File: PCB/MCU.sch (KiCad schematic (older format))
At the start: 18 parts, among them U6 TMS320F28035PAGS, U7 MB85RS16

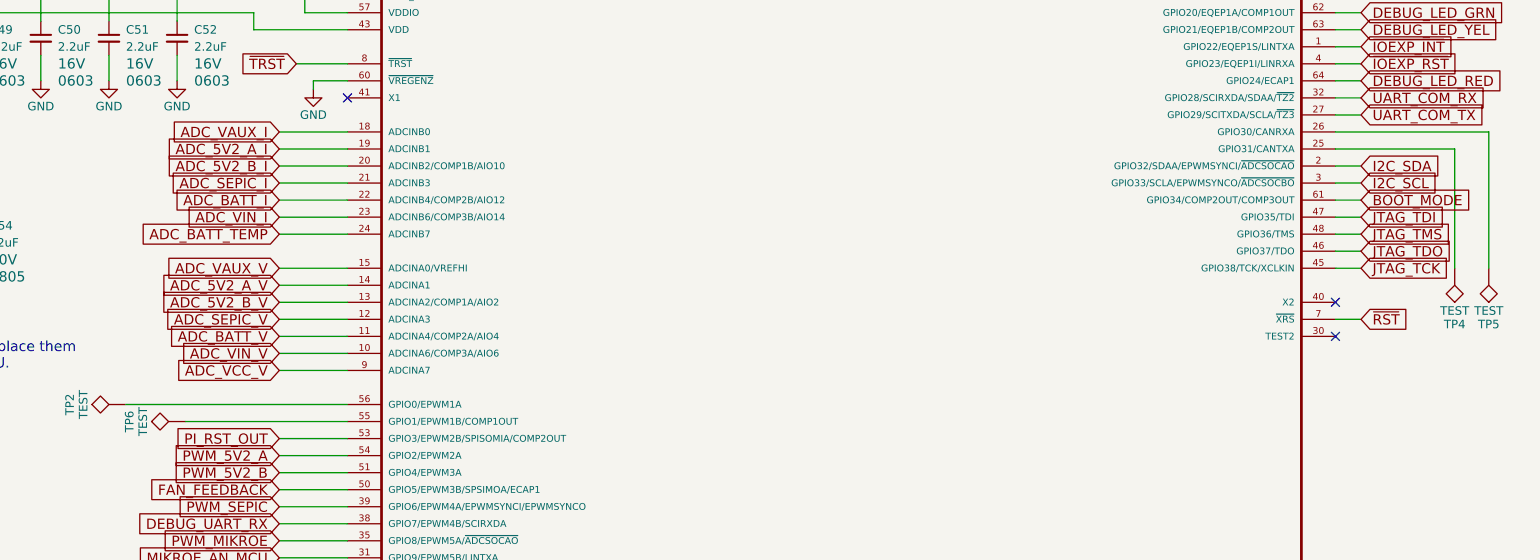
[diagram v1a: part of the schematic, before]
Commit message: Added ELOAD to sch and imported to layout
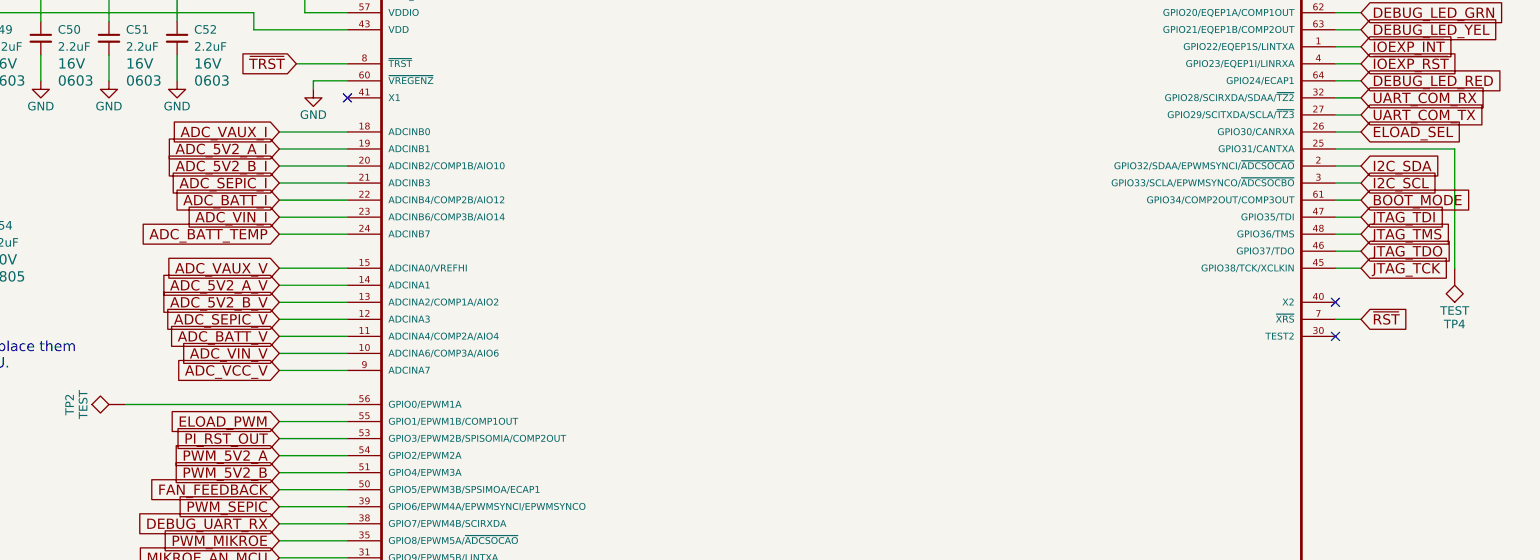
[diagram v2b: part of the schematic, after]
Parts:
- removed TP5, TP6: TEST, Measurement_Points:Measurement_Point_Round-SMD-Pad_Small, symbol TEST
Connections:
- net ELOAD_SEL: now reaches U6.26 (GPIO30/CANRXA)
- net ELOAD_PWM: now reaches U6.55 (GPIO1/EPWM1B/COMP1OUT)
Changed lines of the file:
@@
 $Descr A 11000 8500
 encoding utf-8
-Sheet 6 11
+Sheet 6 12
 Title "MCU"
 Date "2018-06-16"
-Rev "01"
+Rev "02"
 Comp ""
 Comment1 ""
@@
 $EndComp
 $Comp
-L GND #PWR098
+L GND #PWR0101
 U 1 1 5B2621C1
 P 700 1900
-F 0 "#PWR098" H 700 1650 50  0001 C CNN
+F 0 "#PWR0101" H 700 1650 50  0001 C CNN
 F 1 "GND" H 700 1750 50  0000 C CNN
 F 2 "" H 700 1900 50  0001 C CNN
@@
 $EndComp
 $Comp
-L GND #PWR099
+L GND #PWR0102
 U 1 1 5B2621FD
 P 1100 1900
-F 0 "#PWR099" H 1100 1650 50  0001 C CNN
+F 0 "#PWR0102" H 1100 1650 50  0001 C CNN
 F 1 "GND" H 1100 1750 50  0000 C CNN
 F 2 "" H 1100 1900 50  0001 C CNN
@@
 $EndComp
 $Comp
-L GND #PWR0100
+L GND #PWR0103
 U 1 1 5B26221D
 P 1500 1900
-F 0 "#PWR0100" H 1500 1650 50  0001 C CNN
+F 0 "#PWR0103" H 1500 1650 50  0001 C CNN
 F 1 "GND" H 1500 1750 50  0000 C CNN
 F 2 "" H 1500 1900 50  0001 C CNN
@@
 $EndComp
 $Comp
-L GND #PWR0101
+L GND #PWR0104
 U 1 1 5B26223D
 P 1900 1900
-F 0 "#PWR0101" H 1900 1650 50  0001 C CNN
+F 0 "#PWR0104" H 1900 1650 50  0001 C CNN
 F 1 "GND" H 1900 1750 50  0000 C CNN
 F 2 "" H 1900 1900 50  0001 C CNN
@@
 $EndComp
 $Comp
-L GND #PWR0102
+L GND #PWR0105
 U 1 1 5B26225D
 P 2300 1900
-F 0 "#PWR0102" H 2300 1650 50  0001 C CNN
+F 0 "#PWR0105" H 2300 1650 50  0001 C CNN
 F 1 "GND" H 2300 1750 50  0000 C CNN
 F 2 "" H 2300 1900 50  0001 C CNN
@@
 $EndComp
 $Comp
-L GND #PWR0103
+L GND #PWR0106
 U 1 1 5B26227D
 P 2700 1900
-F 0 "#PWR0103" H 2700 1650 50  0001 C CNN
+F 0 "#PWR0106" H 2700 1650 50  0001 C CNN
 F 1 "GND" H 2700 1750 50  0000 C CNN
 F 2 "" H 2700 1900 50  0001 C CNN
@@
 $EndComp
 $Comp
-L GND #PWR0104
+L GND #PWR0107
 U 1 1 5B2622CE
 P 3400 5750
-F 0 "#PWR0104" H 3400 5500 50  0001 C CNN
+F 0 "#PWR0107" H 3400 5500 50  0001 C CNN
 F 1 "GND" H 3400 5600 50  0000 C CNN
 F 2 "" H 3400 5750 50  0001 C CNN
@@
 Connection ~ 2700 1300
 $Comp
-L +3V3 #PWR0105
+L +3V3 #PWR0108
 U 1 1 5B26280D
 P 1900 1000
-F 0 "#PWR0105" H 1900 850 50  0001 C CNN
+F 0 "#PWR0108" H 1900 850 50  0001 C CNN
 F 1 "+3V3" H 1900 1140 50  0000 C CNN
 F 2 "" H 1900 1000 50  0001 C CNN
@@
 $EndComp
 $Comp
-L +3V3 #PWR0106
+L +3V3 #PWR0109
 U 1 1 5B26285E
 P 2300 1000
-F 0 "#PWR0106" H 2300 850 50  0001 C CNN
+F 0 "#PWR0109" H 2300 850 50  0001 C CNN
 F 1 "+3V3" H 2300 1140 50  0000 C CNN
 F 2 "" H 2300 1000 50  0001 C CNN
@@
 	9500 3300 9650 3300
 $Comp
-L GND #PWR0107
+L GND #PWR0110
 U 1 1 5B25830D
 P 3500 1950
-F 0 "#PWR0107" H 3500 1700 50  0001 C CNN
+F 0 "#PWR0110" H 3500 1700 50  0001 C CNN
 F 1 "GND" H 3500 1800 50  0000 C CNN
 F 2 "" H 3500 1950 50  0001 C CNN
@@
 Wire Wire Line
 	10200 1400 9500 1400
-$Comp
-L TEST TP5
-U 1 1 5B258786
-P 10400 3000
-F 0 "TP5" H 10400 3300 50  0000 C BNN
-F 1 "TEST" H 10400 3250 50  0000 C CNN
-F 2 "Measurement_Points:Measurement_Point_Round-SMD-Pad_Small" H 10400 3000 50  0001 C CNN
-F 3 "" H 10400 3000 50  0001 C CNN
-	1    10400 3000
-	-1   0    0    1
-$EndComp
 $Comp
 L TEST TP4
@@
 Wire Wire Line
 	10200 2300 10200 3000
-Wire Wire Line
-	9500 2200 10400 2200
-Wire Wire Line
-	10400 2200 10400 3000
-$Comp
-L TEST TP6
-U 1 1 5B258A6D
-P 2750 3900
-F 0 "TP6" H 2750 4200 50  0000 C BNN
-F 1 "TEST" H 2750 4150 50  0000 C CNN
-F 2 "Measurement_Points:Measurement_Point_Round-SMD-Pad_Small" H 2750 3900 50  0001 C CNN
-F 3 "" H 2750 3900 50  0001 C CNN
-	1    2750 3900
-	0    -1   -1   0
-$EndComp
-Wire Wire Line
-	2750 3900 3700 3900
 $Comp
 L C_Small C48
@@
 $EndComp
 $Comp
-L +3V3 #PWR0108
+L +3V3 #PWR0111
 U 1 1 5B25DAED
 P 800 2500
-F 0 "#PWR0108" H 800 2350 50  0001 C CNN
+F 0 "#PWR0111" H 800 2350 50  0001 C CNN
 F 1 "+3V3" H 800 2640 50  0000 C CNN
 F 2 "" H 800 2500 50  0001 C CNN
@@
 $EndComp
 $Comp
-L +3V3 #PWR0109
+L +3V3 #PWR0112
 U 1 1 5B25DB1F
 P 1500 2500
-F 0 "#PWR0109" H 1500 2350 50  0001 C CNN
+F 0 "#PWR0112" H 1500 2350 50  0001 C CNN
 F 1 "+3V3" H 1500 2640 50  0000 C CNN
 F 2 "" H 1500 2500 50  0001 C CNN
@@
 $EndComp
 $Comp
-L GND #PWR0110
+L GND #PWR0113
 U 1 1 5B25DB51
 P 800 3100
-F 0 "#PWR0110" H 800 2850 50  0001 C CNN
+F 0 "#PWR0113" H 800 2850 50  0001 C CNN
 F 1 "GND" H 800 2950 50  0000 C CNN
 F 2 "" H 800 3100 50  0001 C CNN
@@
 $EndComp
 $Comp
-L GND #PWR0111
+L GND #PWR0114
 U 1 1 5B25DB83
 P 1500 3100
-F 0 "#PWR0111" H 1500 2850 50  0001 C CNN
+F 0 "#PWR0114" H 1500 2850 50  0001 C CNN
 F 1 "GND" H 1500 2950 50  0000 C CNN
 F 2 "" H 1500 3100 50  0001 C CNN
@@
 $EndComp
 $Comp
-L GND #PWR0112
+L GND #PWR0115
 U 1 1 5B2606BF
 P 2900 7500
-F 0 "#PWR0112" H 2900 7250 50  0001 C CNN
+F 0 "#PWR0115" H 2900 7250 50  0001 C CNN
 F 1 "GND" H 2900 7350 50  0000 C CNN
 F 2 "" H 2900 7500 50  0001 C CNN
@@
 $EndComp
 $Comp
-L +3V3 #PWR0113
+L +3V3 #PWR0116
 U 1 1 5B26090E
 P 2900 6550
-F 0 "#PWR0113" H 2900 6400 50  0001 C CNN
+F 0 "#PWR0116" H 2900 6400 50  0001 C CNN
 F 1 "+3V3" H 2900 6690 50  0000 C CNN
 F 2 "" H 2900 6550 50  0001 C CNN
@@
 $EndComp
 $Comp
-L GND #PWR0114
+L GND #PWR0117
 U 1 1 5B260A81
 P 3800 6700
-F 0 "#PWR0114" H 3800 6450 50  0001 C CNN
+F 0 "#PWR0117" H 3800 6450 50  0001 C CNN
 F 1 "GND" H 3800 6550 50  0000 C CNN
 F 2 "" H 3800 6700 50  0001 C CNN
@@
 Connection ~ 1850 7000
 $Comp
-L +3V3 #PWR0115
+L +3V3 #PWR0118
 U 1 1 5B2E79A7
 P 1850 6350
-F 0 "#PWR0115" H 1850 6200 50  0001 C CNN
+F 0 "#PWR0118" H 1850 6200 50  0001 C CNN
 F 1 "+3V3" H 1850 6490 50  0000 C CNN
 F 2 "" H 1850 6350 50  0001 C CNN
@@
 $EndComp
 $Comp
-L +3V3 #PWR0116
+L +3V3 #PWR0119
 U 1 1 5B2E7A2E
 P 2250 6350
-F 0 "#PWR0116" H 2250 6200 50  0001 C CNN
+F 0 "#PWR0119" H 2250 6200 50  0001 C CNN
 F 1 "+3V3" H 2250 6490 50  0000 C CNN
 F 2 "" H 2250 6350 50  0001 C CNN
@@
 	0    -1   -1   0
 $EndComp
+Text GLabel 3300 3900 0    60   Input ~ 0
+ELOAD_PWM
+Wire Wire Line
+	3700 3900 3300 3900
+Text GLabel 9650 2200 2    60   Input ~ 0
+ELOAD_SEL
+Wire Wire Line
+	9650 2200 9500 2200
 $EndSCHEMATC
